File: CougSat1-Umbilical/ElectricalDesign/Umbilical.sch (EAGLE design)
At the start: 54 parts, among them J1 USB, J2 Umbilical, J3 5V input, Q1 CSD16406Q3, Q2 CSD16406Q3, U1 FT230XQ, U2 BQ24650

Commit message: Updated Umbilical
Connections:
- net N$1 renamed FEEDBACK_HIGH
- net N$2 renamed FEEDBACK_LOW
- net !CTS: now also U1.!CTS; no longer U1.CTS
- net !RTS: now also U1.!RTS; no longer U1.RTS
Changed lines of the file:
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@@
 <?xml version="1.0" encoding="utf-8"?>
 <!DOCTYPE eagle SYSTEM "eagle.dtd">
-<eagle version="9.3.2">
+<eagle version="9.4.2">
 <drawing>
 <settings>
@@
 </segment>
 </net>
-<net name="N$1" class="0">
+<net name="FEEDBACK_HIGH" class="0">
 <segment>
 <pinref part="R9" gate="G$1" pin="1"/>
@@
 </segment>
 </net>
-<net name="N$2" class="0">
+<net name="FEEDBACK_LOW" class="0">
 <segment>
 <pinref part="R17" gate="G$1" pin="1"/>
@@
 <segment>
 <pinref part="RN1" gate="D" pin="1"/>
-<pinref part="U1" gate="G$1" pin="CTS"/>
+<pinref part="U1" gate="G$1" pin="!CTS"/>
 <wire x1="193.04" y1="147.32" x2="193.04" y2="119.38" width="0.1524" layer="91"/>
 <wire x1="193.04" y1="119.38" x2="162.56" y2="119.38" width="0.1524" layer="91"/>
@@
 <net name="!RTS" class="0">
 <segment>
-<pinref part="U1" gate="G$1" pin="RTS"/>
+<pinref part="U1" gate="G$1" pin="!RTS"/>
 <pinref part="RN1" gate="C" pin="1"/>
 <wire x1="162.56" y1="121.92" x2="180.34" y2="121.92" width="0.1524" layer="91"/>

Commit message: Updated Umbilical
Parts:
- added LOGO1: SIGNATUREJAYSON, CougsInSpace-Aesthetics:SIGNATUREJAYSON
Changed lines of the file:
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@@
 <?xml version="1.0" encoding="utf-8"?>
 <!DOCTYPE eagle SYSTEM "eagle.dtd">
-<eagle version="9.4.2">
+<eagle version="9.5.0">
 <drawing>
 <settings>
@@
 <part name="R16" library="CougsInSpace-Resistors" deviceset="RES-V" device="-1608" technology="-0" value="0Ω &lt;20mΩ"/>
 <part name="R17" library="CougsInSpace-Resistors" deviceset="RES-V" device="-1608" technology="-0" value="0Ω &lt;20mΩ"/>
+<part name="LOGO1" library="CougsInSpace-Aesthetics" deviceset="SIGNATURE" device="JAYSON"/>
 </parts>
 <sheets>
@@
 <attribute name="TITLE" x="227.33" y="20.32" size="3.81" layer="94" ratio="15" align="bottom-right"/>
 </instance>
+<instance part="LOGO1" gate="G$1" x="218.44" y="53.34" smashed="yes">
+<attribute name="NAME" x="218.44" y="56.134" size="1.778" layer="95" align="bottom-center"/>
+</instance>
 </instances>

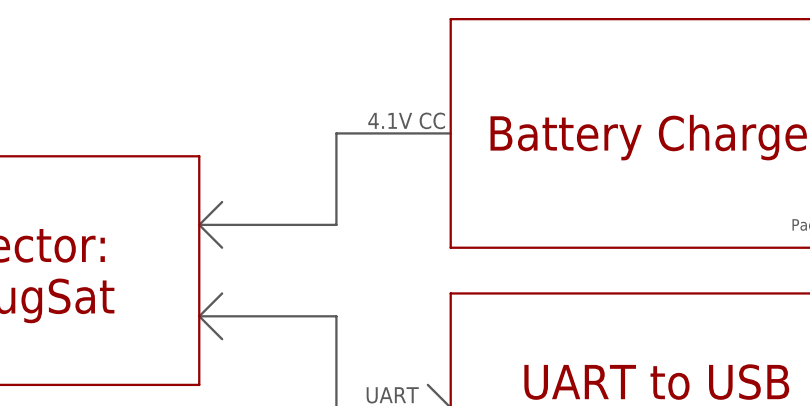
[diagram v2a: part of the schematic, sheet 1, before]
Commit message: Added Three M2 Holes
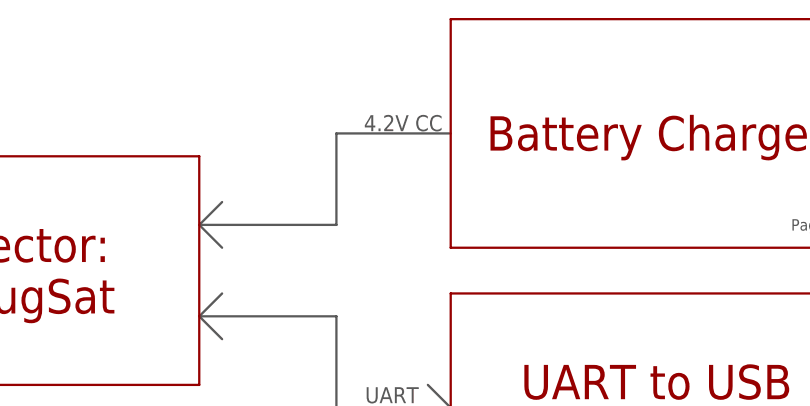
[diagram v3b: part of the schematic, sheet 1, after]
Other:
- note added: "4.2V CC"
- note removed: "4.1V CC"
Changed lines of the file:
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@@
 <wire x1="76.2" y1="96.52" x2="78.74" y2="99.06" width="0.254" layer="97"/>
 <wire x1="76.2" y1="96.52" x2="78.74" y2="93.98" width="0.254" layer="97"/>
-<text x="103.632" y="117.348" size="1.778" layer="97" align="bottom-right">4.1V CC</text>
+<text x="94.488" y="118.872" size="1.778" layer="97" rot="R180" align="bottom-right">4.2V CC</text>
 <text x="100.584" y="86.868" size="1.778" layer="97" align="bottom-right">UART</text>
 <text x="157.48" y="86.614" size="1.778" layer="97" align="bottom-center">USB</text>

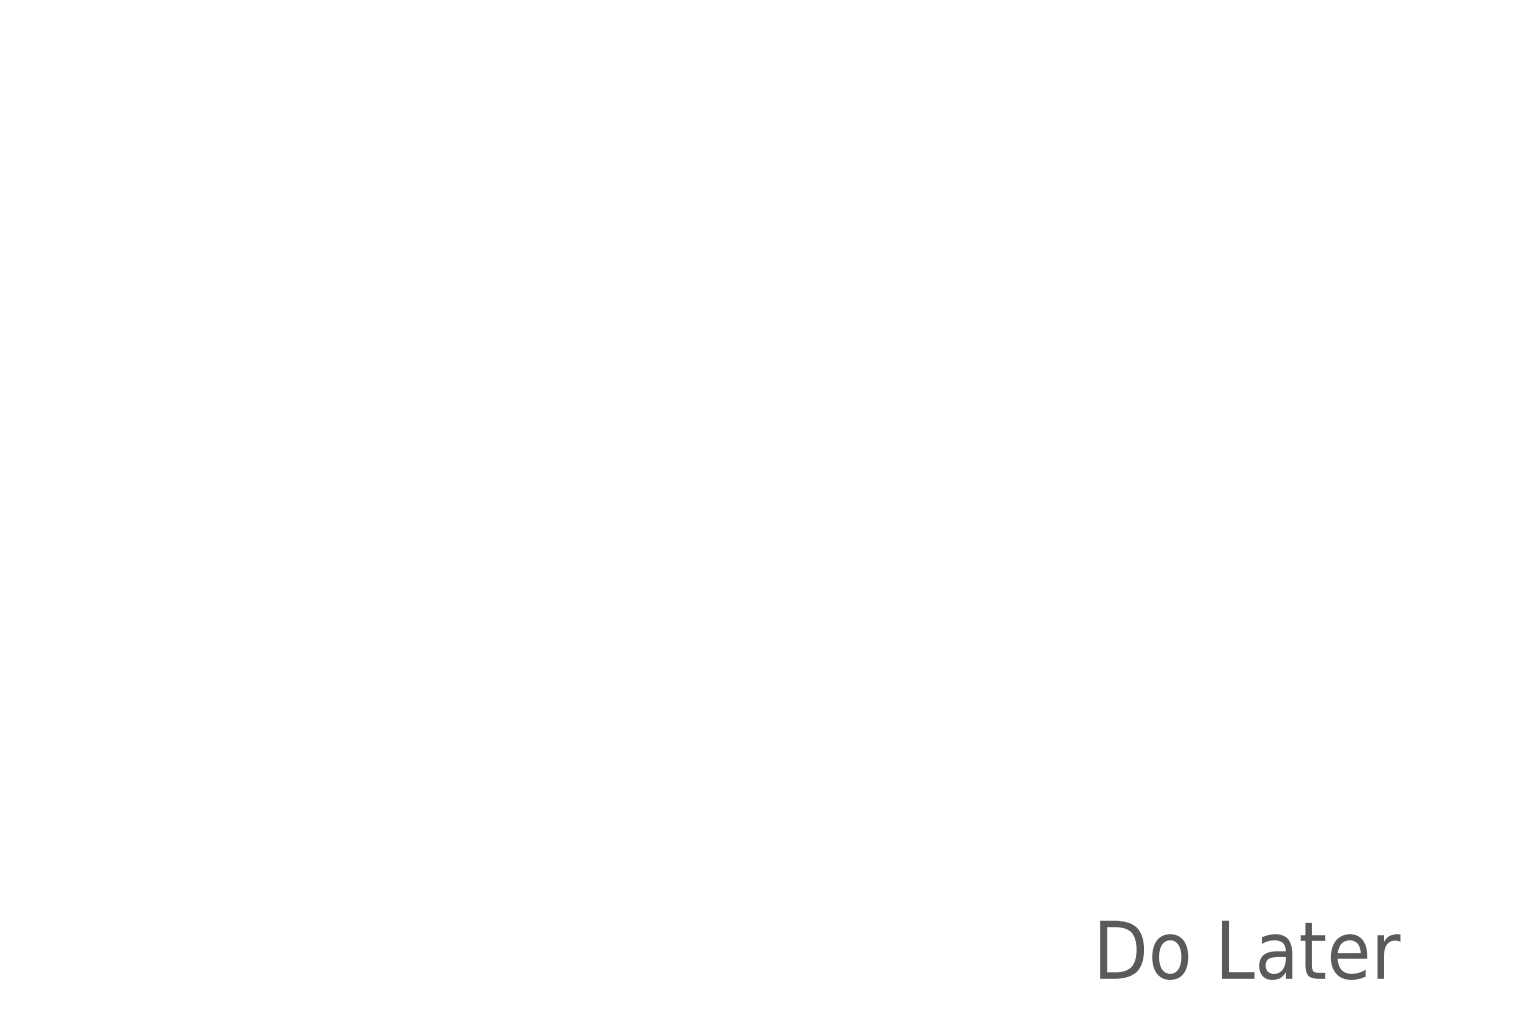
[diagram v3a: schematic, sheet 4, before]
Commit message: Drew Mechanical Page
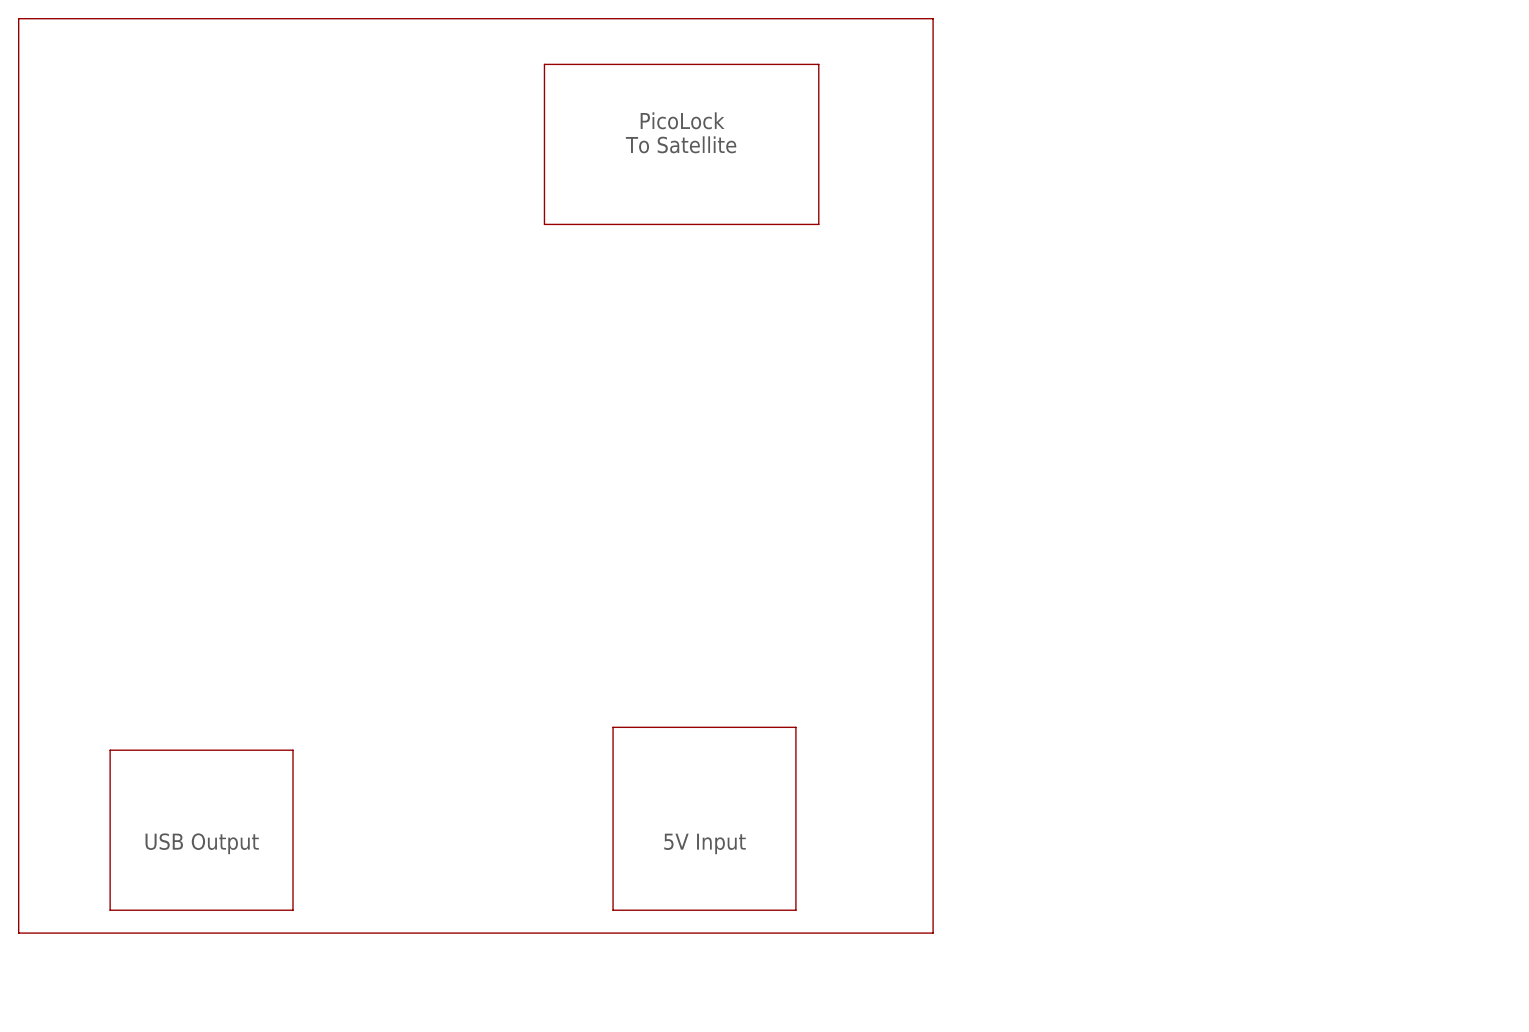
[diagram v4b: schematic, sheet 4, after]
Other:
- note added: "5V Input"
- note added: "PicoLock To Satellite"
- note added: "USB Output"
- note removed: "Do Later"
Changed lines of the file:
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@@
 <sheet>
 <plain>
-<text x="170.18" y="45.72" size="6.4516" layer="97">Do Later</text>
+<wire x1="50.8" y1="152.4" x2="50.8" y2="50.8" width="0.1524" layer="94"/>
+<wire x1="50.8" y1="50.8" x2="152.4" y2="50.8" width="0.1524" layer="94"/>
+<wire x1="152.4" y1="50.8" x2="152.4" y2="152.4" width="0.1524" layer="94"/>
+<wire x1="152.4" y1="152.4" x2="50.8" y2="152.4" width="0.1524" layer="94"/>
+<wire x1="109.22" y1="147.32" x2="109.22" y2="129.54" width="0.1524" layer="94"/>
+<wire x1="109.22" y1="129.54" x2="139.7" y2="129.54" width="0.1524" layer="94"/>
+<wire x1="139.7" y1="129.54" x2="139.7" y2="147.32" width="0.1524" layer="94"/>
+<wire x1="139.7" y1="147.32" x2="109.22" y2="147.32" width="0.1524" layer="94"/>
+<wire x1="116.84" y1="73.66" x2="137.16" y2="73.66" width="0.1524" layer="94"/>
+<wire x1="137.16" y1="73.66" x2="137.16" y2="53.34" width="0.1524" layer="94"/>
+<wire x1="137.16" y1="53.34" x2="116.84" y2="53.34" width="0.1524" layer="94"/>
+<wire x1="116.84" y1="53.34" x2="116.84" y2="73.66" width="0.1524" layer="94"/>
+<wire x1="60.96" y1="71.12" x2="60.96" y2="53.34" width="0.1524" layer="94"/>
+<wire x1="60.96" y1="53.34" x2="81.28" y2="53.34" width="0.1524" layer="94"/>
+<wire x1="81.28" y1="53.34" x2="81.28" y2="71.12" width="0.1524" layer="94"/>
+<wire x1="81.28" y1="71.12" x2="60.96" y2="71.12" width="0.1524" layer="94"/>
+<text x="124.46" y="139.7" size="1.778" layer="97" align="center">PicoLock
+To Satellite</text>
+<text x="127" y="60.96" size="1.778" layer="97" align="center">5V Input</text>
+<text x="71.12" y="60.96" size="1.778" layer="97" align="center">USB Output</text>
 </plain>
 <instances>

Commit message: Fixed The Last Issues
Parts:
- added H1, H2, H3: M3, CougsInSpace-Hardware:MOUNTING_HOLE-3.3
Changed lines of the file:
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@@
 <attribute name="PART_NUMBER" value="68-0009"/>
 <attribute name="PROJECT" value="CougSat Umbilical"/>
-<attribute name="REV" value="1.0.2"/>
+<attribute name="REV" value="1.0.4"/>
 </attributes>
 <variantdefs>
@@
 <part name="R17" library="CougsInSpace-Resistors" deviceset="RES-V" device="-1608" technology="-0" value="0Ω &lt;20mΩ"/>
 <part name="LOGO1" library="CougsInSpace-Aesthetics" deviceset="SIGNATURE" device="JAYSON"/>
+<part name="H1" library="CougsInSpace-Hardware" deviceset="MOUNTING_HOLE" device="-3.3" value="M3"/>
+<part name="H2" library="CougsInSpace-Hardware" deviceset="MOUNTING_HOLE" device="-3.3" value="M3"/>
+<part name="H3" library="CougsInSpace-Hardware" deviceset="MOUNTING_HOLE" device="-3.3" value="M3"/>
 </parts>
 <sheets>
@@
 <attribute name="TITLE" x="227.33" y="20.32" size="3.81" layer="94" ratio="15" align="bottom-right"/>
 </instance>
+<instance part="H1" gate="G$1" x="99.06" y="63.5" smashed="yes">
+<attribute name="NAME" x="99.06" y="66.802" size="1.27" layer="95" align="center"/>
+<attribute name="VALUE" x="99.06" y="60.198" size="1.27" layer="96" align="center"/>
+<attribute name="SKU" x="99.06" y="58.674" size="1.27" layer="97" align="center"/>
+</instance>
+<instance part="H2" gate="G$1" x="63.5" y="144.78" smashed="yes">
+<attribute name="NAME" x="63.5" y="148.082" size="1.27" layer="95" align="center"/>
+<attribute name="VALUE" x="63.5" y="141.478" size="1.27" layer="96" align="center"/>
+<attribute name="SKU" x="63.5" y="139.954" size="1.27" layer="97" align="center"/>
+</instance>
+<instance part="H3" gate="G$1" x="144.78" y="144.78" smashed="yes">
+<attribute name="NAME" x="144.78" y="148.082" size="1.27" layer="95" align="center"/>
+<attribute name="VALUE" x="144.78" y="141.478" size="1.27" layer="96" align="center"/>
+<attribute name="SKU" x="144.78" y="139.954" size="1.27" layer="97" align="center"/>
+</instance>
 </instances>
